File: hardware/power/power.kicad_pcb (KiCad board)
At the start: 2 copper layers, 31.5 x 37 mm, 38 parts, among them J2 Conn_01x04_Pin, J4 Conn_01x04_Pin, P1 USB_C_Plug_USB2.0, U2 ESP32-S3-WROOM-1, U4 MCP1825S

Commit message: redid some traces
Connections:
- ADS131M03 pad 21: GND -> (no net)
- U2 pad 16: unconnected-(U2-IO46-Pad16) -> /USB_{D}+
- U2 pad 17: /USB_{D}+ -> /USB_{D}-
- U2 pad 18: /USB_{D}- -> unconnected-(U2-IO10-Pad18)
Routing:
- net unconnected-(U2-IO46-Pad16): track 0.75 -> 0.00 mm
- net /USB_{D}-: track 9.69 -> 9.08 mm
- net unconnected-(U2-IO10-Pad18): track 0.00 -> 0.53 mm
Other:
- board text added: "write stuff here"

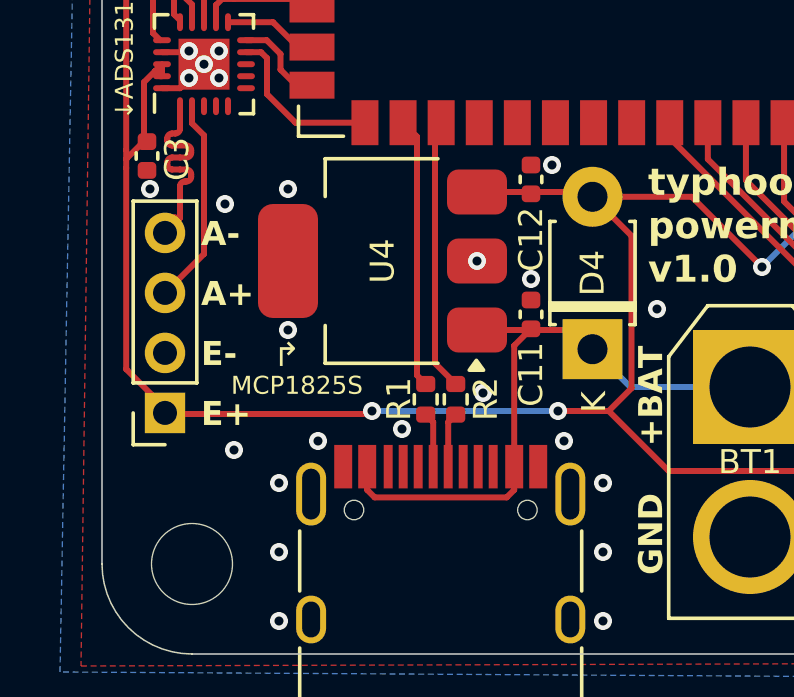
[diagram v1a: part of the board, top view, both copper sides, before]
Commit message: added back silkscreen
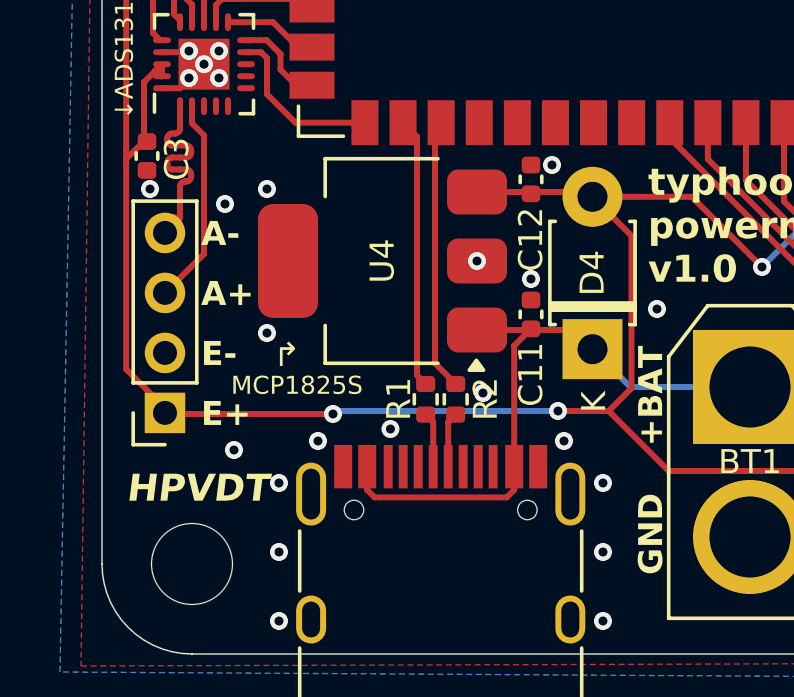
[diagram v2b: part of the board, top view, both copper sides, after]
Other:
- board text added: "- 5V USB-C - 3.7V??? LiPo?? battery - 3.3V wired"
- board text added: "HPVDT"
- board text added: "Power monitor for Typhoon speedbike. Collects crank-based strain and angular velocity data, sent to ESP32 over SPI. ESP32 collects PowerTap pedal data (power, cadence) and communicates with motherboard over BLE."
- board text added: "Powered by ONE OF:"
- board text removed: "3 power sources: - 5V USB - 3.3V wired - external battery"
- board text removed: "write stuff here"
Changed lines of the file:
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@@
 		(layer "Edge.Cuts")
 	)
-	(gr_text "write stuff here"
-		(at 182.9 74.1 0)
+	(gr_text "Power monitor for Typhoon speedbike.\nCollects crank-based strain and angular\nvelocity data, sent to ESP32 over SPI. ESP32\ncollects PowerTap pedal data (power, cadence)\nand communicates with motherboard over BLE."
+		(at 174.5 58.5 90)
 		(layer "B.SilkS")
 		(effects
@@
 		)
 	)
-	(gr_text "3 power sources:\n- 5V USB\n- 3.3V wired\n- external battery"
-		(at 188.1 64.1 0)
+	(gr_text "Powered by ONE OF:"
+		(at 180.3 58.4 90)
+		(layer "B.SilkS")
+		(effects
+			(font
+				(size 0.8 0.8)
+				(thickness 0.16)
+				(bold yes)
+			)
+			(justify left bottom mirror)
+		)
+	)
+	(gr_text "- 5V USB-C\n- 3.7V??? LiPo?? battery\n- 3.3V wired"
+		(at 184.3 58.5 90)
 		(layer "B.SilkS")
 		(effects
@@
 		)
 	)
+	(gr_text "HPVDT"
+		(at 163.4 88.8 0)
+		(layer "F.SilkS")
+		(effects
+			(font
+				(size 0.9 0.9)
+				(thickness 0.2)
+				(bold yes)
+				(italic yes)
+			)
+			(justify left bottom)
+		)
+	)
 	(gr_text "A+"
 		(at 165.9 82.263617 0)
@@
 	)
 	(segment
-		(start 171.5 85.8)
-		(end 164.3 85.8)
-		(width 0.2)
-		(layer "F.Cu")
-		(net 1)
-	)
-	(segment
 		(start 164.57 74.17)
 		(end 164.37 74.37)
@@
 	)
 	(segment
+		(start 170.3 85.8)
+		(end 164.3 85.8)
+		(width 0.2)
+		(layer "F.Cu")
+		(net 1)
+	)
+	(segment
 		(start 187.5 87.7)
 		(end 187.9 88.1)
@@
 	)
 	(segment
-		(start 171.6 85.7)
-		(end 171.5 85.8)
-		(width 0.2)
-		(layer "F.Cu")
-		(net 1)
-	)
-	(segment
 		(start 164.5 67.16)
 		(end 164.5 68.04)
@@
 	)
 	(via
-		(at 171.6 85.7)
+		(at 170.3 85.8)
 		(size 0.6)
 		(drill 0.3)
@@
 	)
 	(segment
+		(start 170.4 85.7)
+		(end 177.8 85.7)
+		(width 0.2)
+		(layer "B.Cu")
+		(net 1)
+	)
+	(segment
 		(start 186.55 78.95)
 		(end 184.6 80.9)
@@
 	)
 	(segment
-		(start 171.6 85.7)
-		(end 177.8 85.7)
+		(start 170.3 85.8)
+		(end 170.4 85.7)
 		(width 0.2)
 		(layer "B.Cu")
@@
 	)
 	(via
-		(at 172.6 86.3)
+		(at 172.214579 86.3)
 		(size 0.6)
 		(drill 0.3)
@@
 	)
 	(via
-		(at 168.8 78.3)
+		(at 168.1 78.3)
 		(size 0.6)
 		(drill 0.3)
@@
 	)
 	(via
-		(at 168.8 83)
+		(at 168.1 83.1)
 		(size 0.6)
 		(drill 0.3)
